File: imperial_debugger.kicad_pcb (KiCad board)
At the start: 4 copper layers, 2 x 7.5 mm, 126 parts, among them J1 USB_B_Micro, J2 Conn_01x04_Male, J3 Conn_01x04_Male, J4 Conn_01x04_Male, J5 Conn_01x06_Male, J6 Conn_01x05_Male, J7 Conn_01x05_Male, J8 Conn_01x05_Male, J9 Conn_01x04_Male, U1 LM2594M-3.3, U10 74LVC1G3157, U11 SP330EEY-L, U12 TXS0104EDR, U13 74LVC1G3157, U14 MAX3222EIPW, U2 93LC54B, U3 FT4232H, U4 74LVC1G3157, U5 SP330EEY-L, U6 74LVC1G3157, U7 TLV75525PDBV, U8 TXS0104EDR, U9 TLV75518PDBV, Y1 12MHz

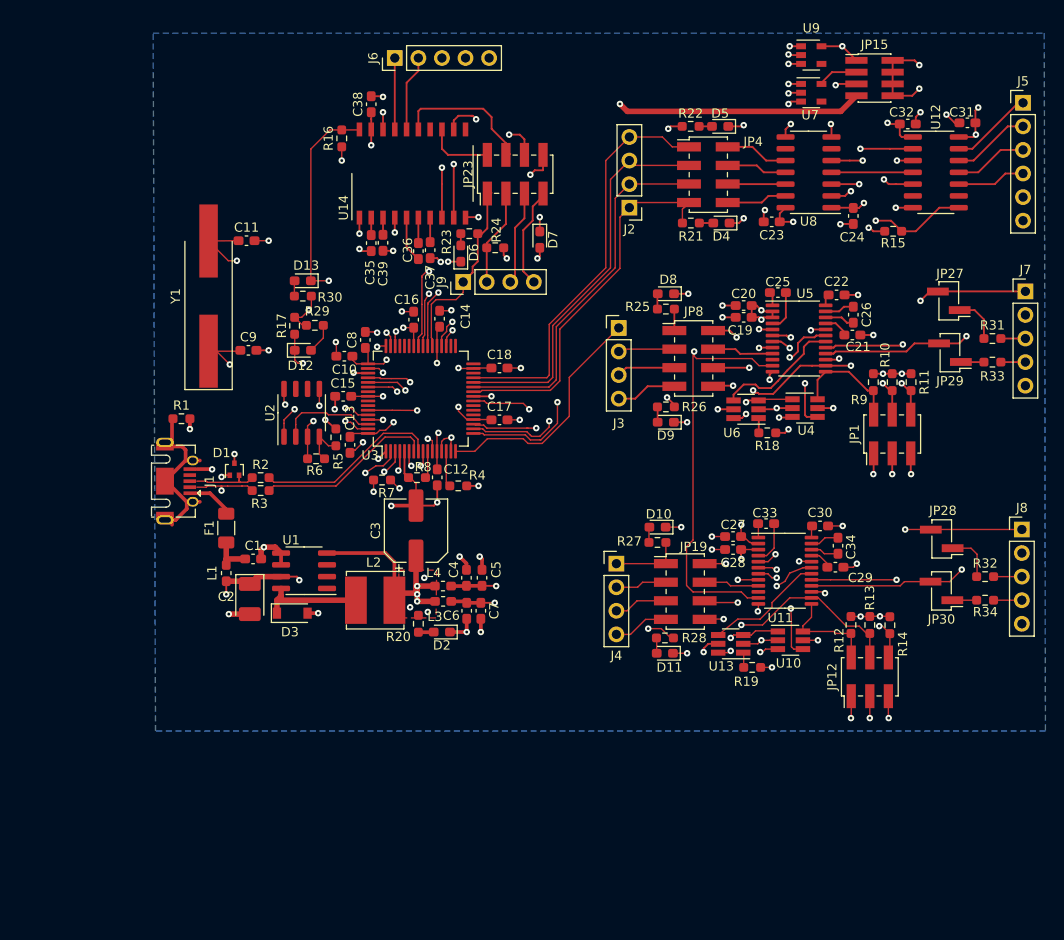
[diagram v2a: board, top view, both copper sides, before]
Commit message: Updates with all the routing and moving to kicad 6.0
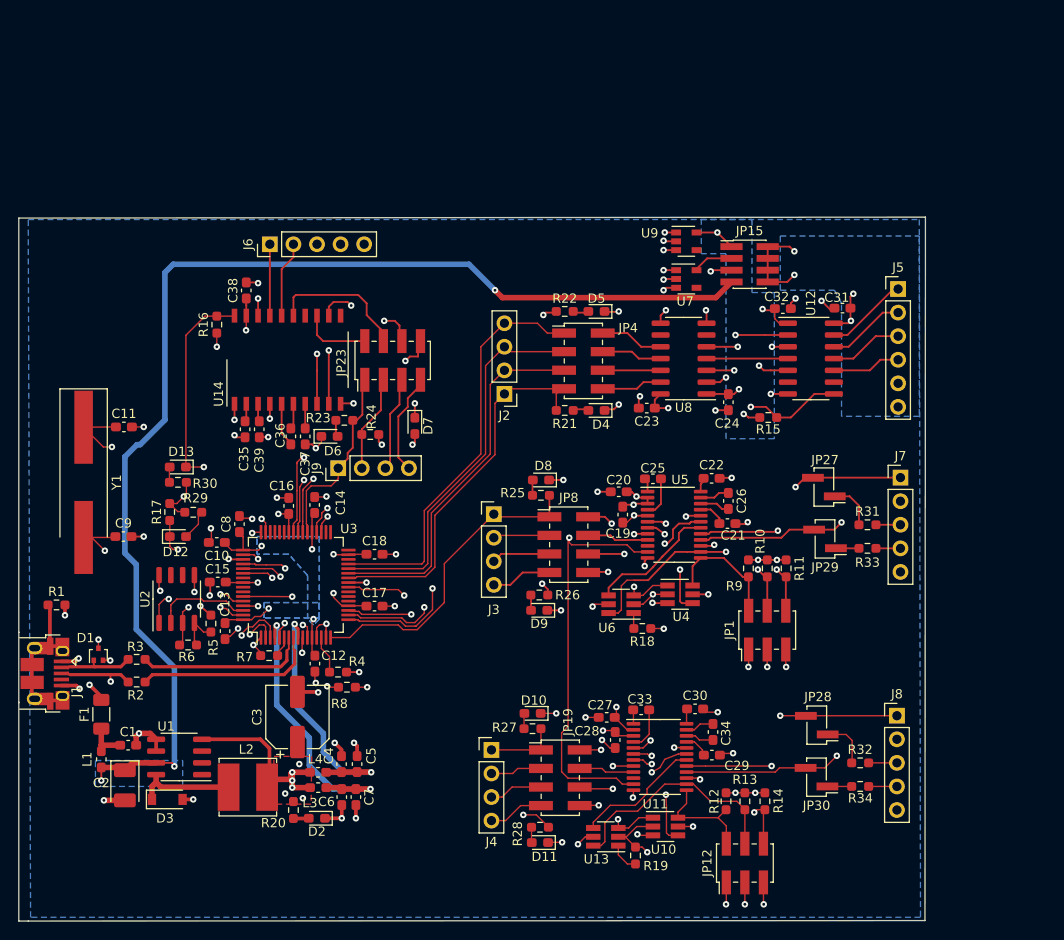
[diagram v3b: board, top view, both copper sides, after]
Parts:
- J1: footprint Connector_USB:USB_Micro-AB_Molex_47590-0001 -> Connector_USB:USB_Micro-B_Amphenol_10103594-0001LF_Horizontal
- moved R2 25.8 mm to (36.8, 127.1)
- moved JP1 25.1 mm to (104.8, 121.5)
- moved R18 25.0 mm to (91.3, 121.3)
- moved U6 24.9 mm to (89.0, 118.7)
- moved C19 24.9 mm to (89.2, 109.0), turned to -90 degrees
- moved U13 24.8 mm to (87.4, 143.7)
- moved D1 24.7 mm to (32.7, 124.1)
- moved J1 24.4 mm to (27.0, 126.2)
- moved R28 24.4 mm to (80.3, 142.7)
- moved D11 24.4 mm to (80.3, 144.3)
- moved D9 24.4 mm to (80.2, 119.3)
- moved R26 24.4 mm to (80.2, 117.7)
- moved C21 24.4 mm to (100.5, 110.0)
- moved L2 24.4 mm to (48.8, 138.4)
- moved R6 24.3 mm to (42.4, 123.1)
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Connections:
- J1 pad 4: Net-(J1-Pad4) -> unconnected-(J1-Pad4)
- U1 pad 1: Net-(U1-Pad1) -> unconnected-(U1-Pad1)
- U1 pad 2: Net-(U1-Pad2) -> unconnected-(U1-Pad2)
- U1 pad 3: Net-(U1-Pad3) -> unconnected-(U1-Pad3)
- U11 pad 10: Net-(U11-Pad10) -> unconnected-(U11-Pad10)
- U2 pad 6: Net-(U2-Pad6) -> unconnected-(U2-Pad6)
- U2 pad 7: Net-(U2-Pad7) -> unconnected-(U2-Pad7)
- U5 pad 10: Net-(U5-Pad10) -> unconnected-(U5-Pad10)
- U7 pad 4: Net-(U7-Pad4) -> unconnected-(U7-Pad4)
- U9 pad 4: Net-(U9-Pad4) -> unconnected-(U9-Pad4)
- Y1 pad 1: Net-(C9-Pad1) -> Net-(C11-Pad1)
- Y1 pad 2: Net-(C11-Pad1) -> Net-(C9-Pad1)
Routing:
- net VPHY: track 7.02 -> 30.7 mm
- net VPLL: track 6.54 -> 27.6 mm
- net Net-(J1-Pad6): track 18.2 -> 12.5 mm
- net ADBUS0: track 28.7 -> 34.4 mm
- net /USB and Power/D+: track 7.02 -> 12.2 mm, vias 0 -> 2
- net Net-(R8-Pad2): track 2.81 -> 7.65 mm, vias 0 -> 2
- net Net-(R7-Pad1): track 6.00 -> 2.24 mm, vias 2 -> 0
- net Net-(F1-Pad2): track 4.35 -> 7.97 mm, vias 0 -> 2
- net GND: track 138.6 -> 141.7 mm, vias 74 -> 72
- net +3V3: track 95.1 -> 92.2 mm
- net Net-(C9-Pad1): track 29.8 -> 31.5 mm
- net Net-(R19-Pad1): track 1.61 -> 3.25 mm
- net CDBUS7: track 1.60 -> 0.00 mm, vias 1 -> 0
- net /USB and Power/D-: track 9.02 -> 10.5 mm, vias 2 -> 0
- net +1V8: track 14.6 -> 13.2 mm
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- added copper zone on B.Cu, net +1V8
- added copper zone on B.Cu, net +3V3
- added copper zone on B.Cu, net /USB and Power/VREGOUT
- added copper zone on In1.Cu, net GND
- added copper zone on B.Cu, net VBUS
- added copper zone on B.Cu, net Vdrive
- removed copper zone on In1.Cu, net +1V8
- removed copper zone on In1.Cu, net +3V3
- removed copper zone on In1.Cu, net /USB and Power/VREGOUT
- removed copper zone on B.Cu, net GND
- removed copper zone on In1.Cu, net VBUS
- removed copper zone on In1.Cu, net VPHY
- removed copper zone on In1.Cu, net VPLL
- removed copper zone on In1.Cu, net Vdrive
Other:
- board size 2 x 7.5 mm -> 97.7 x 75.8 mm
- net class Default removed
- net class Power removed
- net class USB removed

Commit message: After update to kicak 9.0
Signed-off-by: Marc Kelly <mpkelly@achenar.co.uk>
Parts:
- added FID1: Fiducial, Fiducial:Fiducial_1.5mm_Mask3mm, F.Cu at (35.6, 90.3)
- added FID2: Fiducial, Fiducial:Fiducial_1.5mm_Mask3mm, F.Cu at (88.3, 81.9)
- added FID3: Fiducial, Fiducial:Fiducial_1.5mm_Mask3mm, F.Cu at (109.8, 145.7)
- added H1: MountingHole, MountingHole:MountingHole_3.2mm_M3, F.Cu at (32.4, 183.4)
- added H2: MountingHole, MountingHole:MountingHole_3.2mm_M3, F.Cu at (40.4, 183.4)
- added H3: MountingHole, MountingHole:MountingHole_3.2mm_M3, F.Cu at (40.4, 175.5)
- added H4: MountingHole, MountingHole:MountingHole_3.2mm_M3, F.Cu at (32.4, 175.5)
- R10, R11, R12, R13, R14, R9: value 4.7k -> 4k7
- R3: value R10 -> 10R

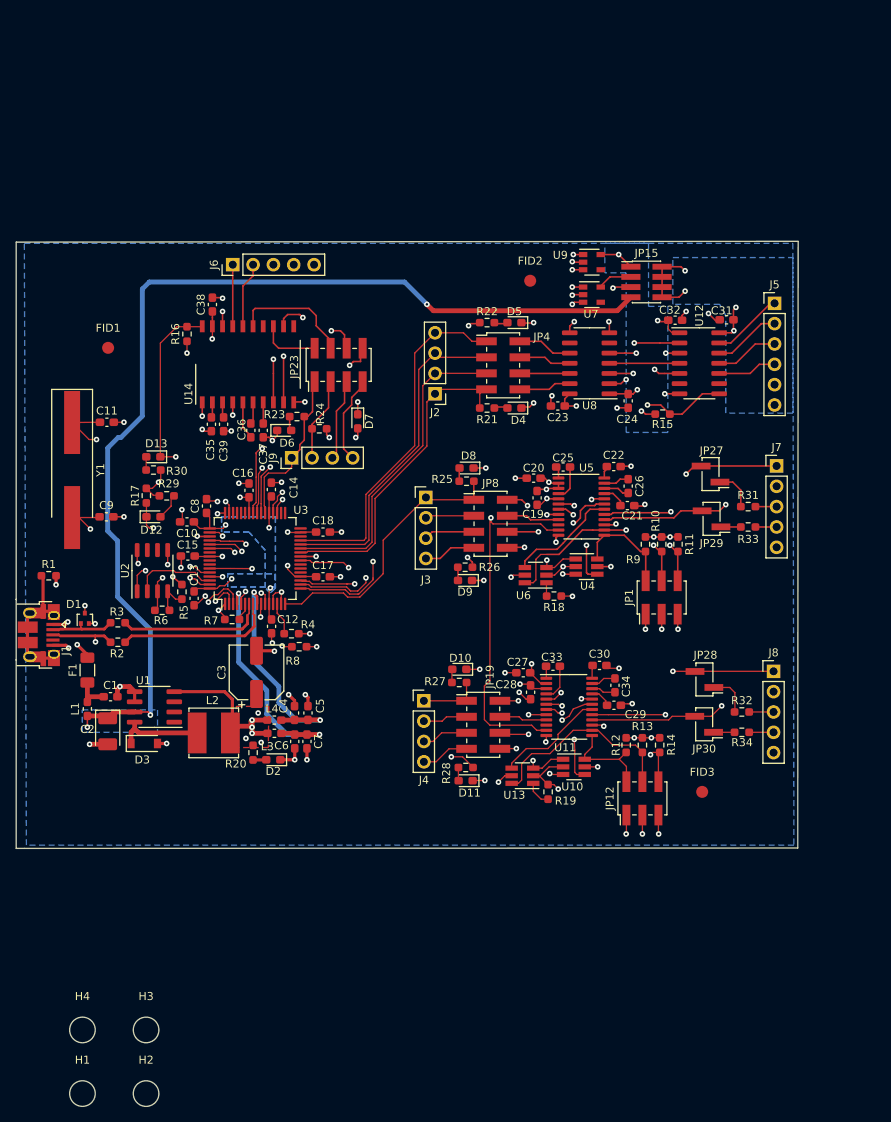
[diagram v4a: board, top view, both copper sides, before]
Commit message: Updated with the new design.
Removed all level translators.
4 sockets, 2x6 pin outputs
New PCB shape and routing
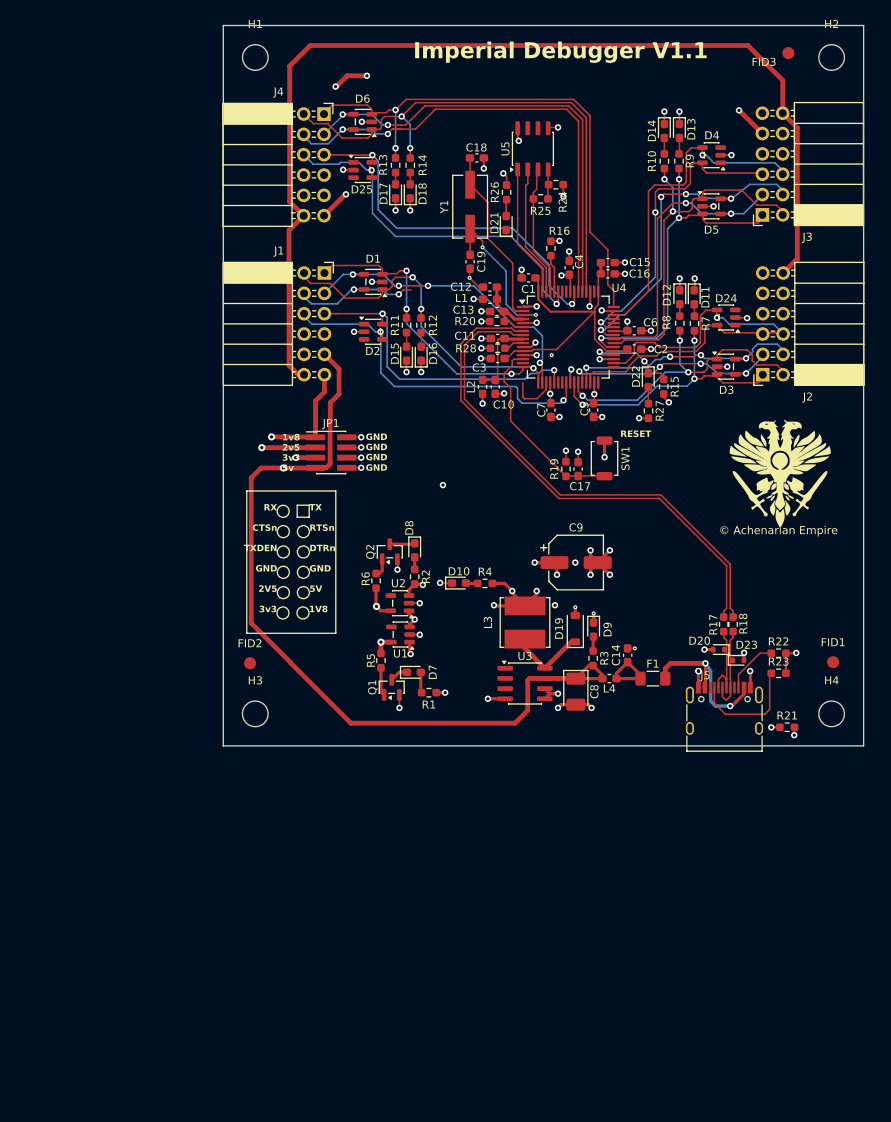
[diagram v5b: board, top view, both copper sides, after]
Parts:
- removed C20, C21, C22, C23, C24, C25, C26, C27, C28, C29, C30, C31, C32, C33, C34, C35, C36, C37, C38, C39: 100nF, Capacitor_SMD:C_0603_1608Metric_Pad1.08x0.95mm_HandSolder
- removed J6, J7, J8: Conn_01x05_Male, Connector_PinHeader_2.54mm:PinHeader_1x05_P2.54mm_Vertical
- removed J9: Conn_01x04_Male, Connector_PinHeader_2.54mm:PinHeader_1x04_P2.54mm_Vertical
- removed JP12: Jumper, Connector_PinHeader_2.00mm:PinHeader_2x03_P2.00mm_Vertical_SMD
- removed JP15: Jumper, Connector_PinHeader_1.27mm:PinHeader_2x04_P1.27mm_Vertical_SMD
- removed JP19, JP23, JP4, JP8: Jumper, Connector_PinHeader_2.00mm:PinHeader_2x04_P2.00mm_Vertical_SMD
- removed JP27, JP28, JP29, JP30: Jumper, Connector_PinHeader_2.00mm:PinHeader_1x02_P2.00mm_Vertical_SMD_Pin1Left
- removed R29, R30: 330R, Resistor_SMD:R_0603_1608Metric_Pad0.98x0.95mm_HandSolder
- removed R31, R32, R33, R34: 120R, Resistor_SMD:R_0603_1608Metric_Pad0.98x0.95mm_HandSolder
- removed U10, U13, U6: 74LVC1G3157, Package_TO_SOT_SMD:SOT-23-6_Handsoldering
- removed U11: SP330EEY-L, Package_SO:TSSOP-24_4.4x7.8mm_P0.65mm
- removed U12, U8: TXS0104EDR, Package_SO:SOIC-14_3.9x8.7mm_P1.27mm
- removed U14: MAX3222EIPW, Package_SO:SO-20_12.8x7.5mm_P1.27mm
- removed U7: TLV75525PDBV, Package_TO_SOT_SMD:SOT-23-5
- removed U9: TLV75518PDBV, Package_TO_SOT_SMD:SOT-23-5
- added D14: G_LED, LED_SMD:LED_0603_1608Metric_Pad1.05x0.95mm_HandSolder, F.Cu at (105.1, 63.2)
- added D15: G_LED, LED_SMD:LED_0603_1608Metric_Pad1.05x0.95mm_HandSolder, F.Cu at (72.9, 91.0)
- added D16: G_LED, LED_SMD:LED_0603_1608Metric_Pad1.05x0.95mm_HandSolder, F.Cu at (74.7, 91.0)
- added D17: G_LED, LED_SMD:LED_0603_1608Metric_Pad1.05x0.95mm_HandSolder, F.Cu at (71.5, 70.7)
- added D18: G_LED, LED_SMD:LED_0603_1608Metric_Pad1.05x0.95mm_HandSolder, F.Cu at (73.4, 70.7)
- added D19: 1A 20V, Diode_SMD:D_SOD-123, F.Cu at (94.0, 125.3)
- added D20: ESD5Zxx, Diode_SMD:D_SOD-523, F.Cu at (111.9, 128.0)
- added D21: G_LED, LED_SMD:LED_0603_1608Metric_Pad1.05x0.95mm_HandSolder, F.Cu at (85.3, 74.7)
- added D22: Or_LED, LED_SMD:LED_0603_1608Metric_Pad1.05x0.95mm_HandSolder, F.Cu at (103.1, 94.3)
- added D23: ESD5Zxx, Diode_SMD:D_SOD-523, F.Cu at (114.4, 129.3)
- added D24: ESDS304, Package_TO_SOT_SMD:SOT-23-5, F.Cu at (112.8, 86.5)
- added D25: ESDS304, Package_TO_SOT_SMD:SOT-23-5, F.Cu at (67.4, 68.1)
- added LOGO1: ~, Achenar_Logos:achenar_logo, F.Cu at (119.5, 106.0)
- added Q1: SI500N025UK-TP, Package_TO_SOT_SMD:SOT-23, F.Cu at (71.0, 132.7)
- added Q2: SI500N025UK-TP, Package_TO_SOT_SMD:SOT-23, F.Cu at (70.8, 115.7)
- added SW1: ResetButton, Button_Switch_SMD:SW_SPST_TS-1088-xR020, F.Cu at (97.6, 104.1)
- C1: value 10nf -> 100nF
- C10, C12: value 100nF -> 4.7uF
- C14: value 100nF -> 10nf
- C16: value 100nF -> 3.3uF
- C2: value 68uF -> 100nF; footprint Capacitor_Tantalum_SMD:CP_EIA-3528-21_Kemet-B_Pad1.50x2.35mm_HandSolder -> Capacitor_SMD:C_0603_1608Metric_Pad1.08x0.95mm_HandSolder
- C3: value 120uF -> 100nF; footprint Capacitor_SMD:CP_Elec_6.3x5.7 -> Capacitor_SMD:C_0603_1608Metric_Pad1.08x0.95mm_HandSolder
- C4, C6: value 4.7uF -> 100nF
- C8: value 3.3uF -> 68uF; footprint Capacitor_SMD:C_0603_1608Metric_Pad1.08x0.95mm_HandSolder -> Capacitor_Tantalum_SMD:CP_EIA-3528-21_Kemet-B_HandSolder
- C9: value 100nF -> 120uF; footprint Capacitor_SMD:C_0603_1608Metric_Pad1.08x0.95mm_HandSolder -> Capacitor_SMD:CP_Elec_6.3x5.7
- D1: value RClamp0582BQ -> ESDS304; footprint Package_TO_SOT_SMD:SOT-416 -> Package_TO_SOT_SMD:SOT-23-5
- D10, D7, D8, D9: value G_LED -> Y_LED
- D13: value Or_LED -> G_LED
- D2, D4, D5, D6: value G_LED -> ESDS304; footprint LED_SMD:LED_0603_1608Metric_Pad1.05x0.95mm_HandSolder -> Package_TO_SOT_SMD:SOT-23-5
- D3: value 1A 20V -> ESDS304; footprint Diode_SMD:D_SOD-123 -> Package_TO_SOT_SMD:SOT-23-5
- J1: value USB_B_Micro -> Conn_02x06_Odd_Even; footprint Connector_USB:USB_Micro-B_Amphenol_10103594-0001LF_Horizontal -> Connector_PinSocket_2.54mm:PinSocket_2x06_P2.54mm_Horizontal
- J2, J3, J4: value Conn_01x04_Male -> Conn_02x06_Odd_Even; footprint Connector_PinHeader_2.54mm:PinHeader_1x04_P2.54mm_Vertical -> Connector_PinSocket_2.54mm:PinSocket_2x06_P2.54mm_Horizontal
- J5: value Conn_01x06_Male -> USB_C_Receptacle_USB2.0_14P; footprint Connector_PinHeader_2.54mm:PinHeader_1x06_P2.54mm_Vertical -> Connector_USB:USB_C_Receptacle_HRO_TYPE-C-31-M-12
- JP1: footprint Connector_PinHeader_2.00mm:PinHeader_2x03_P2.00mm_Vertical_SMD -> Connector_PinHeader_1.27mm:PinHeader_2x04_P1.27mm_Vertical_SMD
- L2: value SRN6045-101M -> 330R/0.5A; footprint Inductor_SMD:L_Bourns_SRN6045TA -> Inductor_SMD:L_0603_1608Metric_Pad1.05x0.95mm_HandSolder
- L3: value 330R/0.5A -> SRN6045-101M; footprint Inductor_SMD:L_0603_1608Metric_Pad1.05x0.95mm_HandSolder -> Inductor_SMD:L_Bourns_SRN6045TA
- R1, R8: value 0R -> 330R
- R10, R11, R12, R13, R14, R9: value 4k7 -> 330R
- R17, R18: value 4k7 -> 10R
- R19: value 4k7 -> 10k
- R2, R3: value 10R -> 330R
- R20: value 330R -> 12k/1%
- R21, R28: value 330R -> 0R
- R22, R23: value 330R -> 5k1
- R24: value 330R -> 10k
- R25: value 330R -> 2K
- R4, R5: value 10k -> 330R
- R6: value 2K -> 330R
- R7: value 12k/1% -> 330R
- U1: value LM2594M-3.3 -> TLV75525PDBV; footprint Package_SO:SOIC-8_3.9x4.9mm_P1.27mm -> Package_TO_SOT_SMD:SOT-23-5
- U2: value 93LC54B -> TLV75518PDBV; footprint Package_SO:SO-8_3.9x4.9mm_P1.27mm -> Package_TO_SOT_SMD:SOT-23-5
- U3: value FT4232H -> LM2594M-3.3; footprint Package_QFP:LQFP-64_10x10mm_P0.5mm -> Package_SO:SOIC-8_3.9x4.9mm_P1.27mm
- U4: value 74LVC1G3157 -> FT4232H; footprint Package_TO_SOT_SMD:SOT-23-6_Handsoldering -> Package_QFP:LQFP-64_10x10mm_P0.5mm
- U5: value SP330EEY-L -> 93LC54B; footprint Package_SO:TSSOP-24_4.4x7.8mm_P0.65mm -> Package_SO:SO-8_3.9x4.9mm_P1.27mm
- Y1: value 12MHz -> ABLS7M2-12.000MHZ-D2Y-T; footprint Crystal:Crystal_SMD_HC49-SD_HandSoldering -> Crystal:Crystal_SMD_ECS_CSM3X-2Pin_7.6x4.1mm
- moved H2 155.2 mm to (126.0, 54.0)
- moved H1 131.2 mm to (54.0, 54.0)
- moved H4 101.6 mm to (126.0, 136.0)
- moved FID1 98.7 mm to (126.2, 129.5)
- moved FID3 92.9 mm to (120.6, 53.4), turned to -90 degrees
- moved D3 86.6 mm to (112.8, 92.6)
- moved C2 81.3 mm to (101.3, 90.4), turned to 0 degrees
- moved R14 78.9 mm to (73.4, 67.5), turned to 90 degrees
- moved R13 78.7 mm to (71.5, 67.5), turned to 90 degrees
- moved D13 77.3 mm to (107.0, 63.2), turned to -90 degrees
- moved J4 74.4 mm to (62.6, 61.1)
- moved C1 73.9 mm to (88.1, 81.5), turned to 180 degrees
- moved R17 73.9 mm to (112.5, 124.8)
- moved L1 71.8 mm to (83.3, 84.2), turned to 0 degrees
- moved D12 71.3 mm to (107.0, 83.9), turned to -90 degrees
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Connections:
- C1 pad 1: Net-(C1-Pad1) -> /USB and Power/VREGOUT
- C10 pad 1: /USB and Power/VREGOUT -> VPLL
- C11 pad 1: Net-(C11-Pad1) -> VPLL
- C12 pad 1: /USB and Power/VREGOUT -> VPHY
- C13 pad 1: /USB and Power/VREGOUT -> VPHY
- C14 pad 1: /USB and Power/VREGOUT -> Net-(C14-Pad1)
- C15 pad 1: +3V3 -> /USB and Power/VREGOUT
- C16 pad 1: +3V3 -> /USB and Power/VREGOUT
- C17 pad 1: +3V3 -> /USB and Power/RESET#
- C18 pad 1: +3V3 -> Net-(U4-OSCI)
- C19 pad 1: +3V3 -> Net-(U4-OSCO)
- C2 pad 1: VBUS -> /USB and Power/VREGOUT
- C3 pad 1: +3V3 -> /USB and Power/VREGOUT
- C4 pad 1: VPLL -> +3V3
- C5 pad 1: VPLL -> +3V3
- C6 pad 1: VPHY -> +3V3
- C7 pad 1: VPHY -> +3V3
- C8 pad 1: /USB and Power/VREGOUT -> VBUS
- C9 pad 1: Net-(C9-Pad1) -> +3V3
- D1 pad 1: /USB and Power/D- -> ADBUS1
- D1 pad 2: /USB and Power/D+ -> GND
- D1 pad 3: GND -> ADBUS0
- D10 pad 2: Net-(D10-Pad2) -> Net-(D10-A)
- D11 pad 2: Net-(D11-Pad2) -> Net-(D11-A)
- D12 pad 1: PWREN# -> GND
- D12 pad 2: Net-(D12-Pad2) -> Net-(D12-A)
- D13 pad 1: SUSPEND# -> GND
- D13 pad 2: Net-(D13-Pad2) -> Net-(D13-A)
- D2 pad 1: GND -> unconnected-(D2-K-Pad1)
- D2 pad 2: Net-(D2-Pad2) -> GND
- D3 pad 1: Net-(D3-Pad1) -> BDBUS1
- D4 pad 1: GND -> unconnected-(D4-K-Pad1)
- D4 pad 2: Net-(D4-Pad2) -> GND
- D5 pad 1: GND -> CDBUS1
- D5 pad 2: Net-(D5-Pad2) -> GND
- D6 pad 1: GND -> DDBUS1
- D6 pad 2: Net-(D6-Pad2) -> GND
- D7 pad 1: GND -> Net-(D7-K)
- D7 pad 2: Net-(D7-Pad2) -> Net-(D7-A)
- D8 pad 1: GND -> Net-(D8-K)
- D8 pad 2: Net-(D8-Pad2) -> Net-(D8-A)
- D9 pad 2: Net-(D9-Pad2) -> Net-(D9-A)
- F1 pad 1: Net-(C1-Pad1) -> Net-(C14-Pad1)
- J1 pad 1: Net-(F1-Pad2) -> ADBUS0
- J1 pad 2: /USB and Power/D- -> ADBUS1
- J1 pad 3: /USB and Power/D+ -> ADBUS2
- J1 pad 4: unconnected-(J1-Pad4) -> ADBUS3
- J1 pad 5: GND -> ADBUS4
- J1 pad 6: Net-(J1-Pad6) -> ADBUS7
- J3 pad 1: ADBUS0 -> CDBUS0
- J3 pad 2: ADBUS1 -> CDBUS1
- J3 pad 3: ADBUS2 -> CDBUS2
- J3 pad 4: ADBUS3 -> CDBUS3
- JP1 pad 1: GND -> +1V8
- JP1 pad 2: /Transceivers/RS323n_3 -> GND
- JP1 pad 3: GND -> +2V5
- JP1 pad 4: /Transceivers/FULLn_3 -> GND
- JP1 pad 5: GND -> +3V3
- JP1 pad 6: Net-(JP1-Pad6) -> GND
- L1 pad 1: VBUS -> +3V3
- L1 pad 2: Net-(C1-Pad1) -> VPHY
- L2 pad 1: Net-(D3-Pad1) -> +3V3
- L2 pad 2: +3V3 -> VPLL
- L3 pad 1: +3V3 -> Net-(D19-K)
- L3 pad 2: VPHY -> +3V3
- L4 pad 1: +3V3 -> VBUS
- L4 pad 2: VPLL -> Net-(C14-Pad1)
- R1 pad 1: Net-(J1-Pad6) -> Net-(D7-A)
- R1 pad 2: GND -> +3V3
- R10 pad 1: +3V3 -> Net-(D14-A)
- R10 pad 2: /Transceivers/FULLn_3 -> CDBUS1
- R11 pad 1: +3V3 -> Net-(D15-A)
- R11 pad 2: Net-(JP1-Pad6) -> ADBUS0
- R12 pad 1: +3V3 -> Net-(D16-A)
- R12 pad 2: /Transceivers/RS323n_4 -> ADBUS1
- R13 pad 1: +3V3 -> Net-(D17-A)
- R13 pad 2: /Transceivers/FULLn_4 -> DDBUS0
- R14 pad 1: +3V3 -> Net-(D18-A)
- R14 pad 2: Net-(JP12-Pad6) -> DDBUS1
- R15 pad 1: +1V8 -> +3V3
- R15 pad 2: Net-(R15-Pad2) -> SUSPEND#
- R16 pad 2: SUSPEND# -> PWREN#
- R17 pad 1: +3V3 -> /USB and Power/D_N
- R17 pad 2: PWREN# -> /USB and Power/D-
- R18 pad 1: Net-(R18-Pad1) -> /USB and Power/D_P
- R18 pad 2: GND -> /USB and Power/D+
- R19 pad 1: Net-(R19-Pad1) -> /USB and Power/RESET#
- R19 pad 2: GND -> +3V3
- R2 pad 1: /USB and Power/D_P -> Net-(D8-A)
- R2 pad 2: /USB and Power/D+ -> +3V3
- R20 pad 1: Net-(D2-Pad2) -> Net-(U4-REF)
- R20 pad 2: +3V3 -> GND
- R21 pad 1: Net-(D4-Pad2) -> Net-(J5-SHIELD)
- R21 pad 2: BDBUS0 -> GND
- R22 pad 1: Net-(D5-Pad2) -> Net-(J5-CC2)
- R22 pad 2: BDBUS1 -> GND
- R23 pad 1: Net-(D6-Pad2) -> Net-(J5-CC1)
- R23 pad 2: CDBUS0 -> GND
- R24 pad 1: Net-(D7-Pad2) -> Net-(U5-DO)
- R24 pad 2: CDBUS1 -> +3V3
- R25 pad 1: Net-(D8-Pad2) -> Net-(U4-EEDATA)
- R25 pad 2: ADBUS0 -> Net-(U5-DO)
- R26 pad 1: Net-(D9-Pad2) -> Net-(D21-A)
- R26 pad 2: ADBUS1 -> +3V3
- R27 pad 1: Net-(D10-Pad2) -> Net-(D22-A)
- R27 pad 2: DDBUS0 -> +3V3
- R28 pad 1: Net-(D11-Pad2) -> GND
- R28 pad 2: DDBUS1 -> Net-(U4-AGND)
- R3 pad 1: /USB and Power/D_N -> Net-(D9-A)
- R3 pad 2: /USB and Power/D- -> VBUS
- R4 pad 1: /USB and Power/RESET# -> Net-(D10-A)
- R5 pad 1: Net-(R5-Pad1) -> +2V5
- R5 pad 2: +3V3 -> Net-(Q1-G)
- R6 pad 1: Net-(R6-Pad1) -> +1V8
- R6 pad 2: Net-(R5-Pad1) -> Net-(Q2-G)
- R7 pad 1: Net-(R7-Pad1) -> Net-(D11-A)
- R7 pad 2: GND -> BDBUS0
- R8 pad 1: GND -> Net-(D12-A)
- R8 pad 2: Net-(R8-Pad2) -> BDBUS1
- R9 pad 1: +3V3 -> Net-(D13-A)
- R9 pad 2: /Transceivers/RS323n_3 -> CDBUS0
- U1 pad 1: unconnected-(U1-Pad1) -> +3V3
- U1 pad 2: unconnected-(U1-Pad2) -> GND
- U1 pad 3: unconnected-(U1-Pad3) -> +3V3
- U1 pad 4: +3V3 -> unconnected-(U1-NC-Pad4)
- U1 pad 5: GND -> +2V5
- U2 pad 1: Net-(U2-Pad1) -> +3V3
- U2 pad 2: Net-(U2-Pad2) -> GND
- U2 pad 3: Net-(R6-Pad1) -> +3V3
- U2 pad 4: Net-(R5-Pad1) -> unconnected-(U2-NC-Pad4)
- U2 pad 5: GND -> +1V8
- U3 pad 1: GND -> unconnected-(U3-NC-Pad1)
- U3 pad 2: Net-(C9-Pad1) -> unconnected-(U3-NC-Pad2)
- U3 pad 3: Net-(C11-Pad1) -> unconnected-(U3-NC-Pad3)
- U3 pad 4: VPHY -> +3V3
- U3 pad 6: Net-(R7-Pad1) -> GND
- U3 pad 7: /USB and Power/D_N -> VBUS
- U3 pad 8: /USB and Power/D_P -> Net-(D19-K)
- U4 pad 1: ADBUS7 -> GND
- U4 pad 2: GND -> Net-(U4-OSCI)
- U4 pad 3: /Transceivers/RTSn_3 -> Net-(U4-OSCO)
- U4 pad 4: /Transceivers/T2IN_3 -> VPHY
- U4 pad 5: +3V3 -> GND
- U4 pad 6: /Transceivers/RS323n_3 -> Net-(U4-REF)
- U5 pad 1: Net-(C25-Pad2) -> Net-(U4-EECS)
- U5 pad 2: +3V3 -> Net-(U4-EECLK)
- U5 pad 3: +3V3 -> Net-(U4-EEDATA)
- U5 pad 4: Net-(C25-Pad1) -> Net-(U5-DO)
- U5 pad 6: /Transceivers/PORT_3_TXD -> unconnected-(U5-NC-Pad6)
- U5 pad 7: /Transceivers/PORT_3_RTS -> unconnected-(U5-NC-Pad7)
- U5 pad 8: /Transceivers/CTSn_3 -> +3V3
- Y1 pad 1: Net-(C11-Pad1) -> Net-(U4-OSCO)
- Y1 pad 2: Net-(C9-Pad1) -> Net-(U4-OSCI)
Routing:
- net +2V5: track 4.37 -> 193.8 mm, vias 0 -> 2
- net +1V8: track 13.2 -> 173.0 mm, vias 4 -> 3
- net +3V3: track 92.2 -> 215.9 mm, vias 35 -> 27
- net SUSPEND#: track 112.2 -> 12.3 mm, vias 3 -> 2
- net VBUS: track 131.0 -> 221.5 mm, vias 3 -> 4
- net DDBUS4: track 0.00 -> 46.5 mm, vias 0 -> 2
- net /USB and Power/D_N: track 18.4 -> 64.1 mm
- net /USB and Power/D_P: track 19.8 -> 63.4 mm
- net Net-(C11-Pad1): track 42.8 -> 0.00 mm, vias 2 -> 0
- net CDBUS7: track 0.00 -> 40.9 mm, vias 0 -> 1
- net ADBUS4: track 0.00 -> 39.0 mm, vias 0 -> 2
- net CDBUS4: track 0.00 -> 38.8 mm, vias 0 -> 2
- net GND: track 141.7 -> 106.9 mm, vias 72 -> 69
- net /Transceivers/PORT_4_RTS: track 32.5 -> 0.00 mm, vias 1 -> 0
- net /Transceivers/PORT_3_RTS: track 31.8 -> 0.00 mm, vias 1 -> 0
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- added copper zone on In2.Cu, net +3V3
- added copper zone on In1.Cu, net Net-(J5-SHIELD)
- removed copper zone on B.Cu, net +1V8
- removed copper zone on B.Cu, net +3V3
- removed copper zone on F.Cu, net +3V3
- removed copper zone on B.Cu, net /USB and Power/VREGOUT
- removed copper zone on B.Cu, net VBUS
- removed copper zone on B.Cu, net Vdrive
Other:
- board size 97.7 x 75.8 mm -> 80 x 90 mm
- board text added: "1V8"
- board text added: "1v8"
- board text added: "2V5"
- board text added: "2v5"
- board text added: "3v3"
- board text added: "5V"
- board text added: "5v"
- board text added: "CTSn"
- board text added: "DTRn"
- board text added: "GND"
- board text added: "Imperial Debugger V${REVISION}"
- board text added: "RESET"
- board text added: "RTSn"
- board text added: "RX"
- board text added: "TX"
- board text added: "TXDEN"

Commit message: Add some info to the master document
Signed-off-by: Marc Kelly <mpkelly@achenar.co.uk>
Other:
- board text added: "Sub Module need to be 15.3+4.6 = 19.9 mm So will go for 19.4 mm wide for the sub modules."
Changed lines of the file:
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@@
+	)
+	(gr_rect
+		(start 145.4404 77.5994)
+		(end 195.4404 96.9994)
+		(stroke
+			(width 0.1)
+			(type solid)
+		)
+		(fill no)
+		(layer "Dwgs.User")
+	)
+	(gr_rect
+		(start 145.434 57.635)
+		(end 195.434 77.035)
+		(stroke
+			(width 0.1)
+			(type solid)
+		)
+		(fill no)
+		(layer "Dwgs.User")
 	)
 	(gr_rect
@@
 		)
 	)
+	(gr_text "Sub Module need to be 15.3+4.6 = 19.9 mm\n So will go for 19.4 mm wide for the sub modules."
+		(at 136.2964 56.769 0)
+		(layer "Dwgs.User")
+		(effects
+			(font
+				(size 1 1)
+				(thickness 0.15)
+			)
+			(justify left bottom)
+		)
+	)
+	(dimension
+		(type orthogonal)
+		(layer "Dwgs.User")
+		(pts
+			(xy 135.7376 74.99) (xy 136.61004 59.610569)
+		)
+		(height 0)
+		(orientation 1)
+		(format
+			(prefix "")
+			(suffix "")
+			(units 3)
+			(units_format 1)
+			(precision 4)
+		)
+		(style
+			(thickness 0.1)
+			(arrow_length 1.27)
+			(text_position_mode 0)
+			(arrow_direction outward)
+			(extension_height 0.58642)
+			(extension_offset 0.5)
+			(keep_text_aligned yes)
+		)
+		(gr_text "15.3794 mm"
+			(at 134.5876 67.300284 90)
+			(layer "Dwgs.User")
+			(effects
+				(font
+					(size 1 1)
+					(thickness 0.15)
+				)
+			)
+		)
+	)
+	(dimension
+		(type orthogonal)
+		(layer "Dwgs.User")
+		(pts
+			(xy 133.479591 79.5944) (xy 133.618874 74.99)
+		)
+		(height 0)
+		(orientation 1)
+		(format
+			(prefix "")
+			(suffix "")
+			(units 3)
+			(units_format 1)
+			(precision 4)
+		)
+		(style
+			(thickness 0.1)
+			(arrow_length 1.27)
+			(text_position_mode 0)
+			(arrow_direction outward)
+			(extension_height 0.58642)
+			(extension_offset 0.5)
+			(keep_text_aligned yes)
+		)
+		(gr_text "4.6044 mm"
+			(at 132.329591 77.2922 90)
+			(layer "Dwgs.User")
+			(effects
+				(font
+					(size 1 1)
+					(thickness 0.15)
+				)
+			)
+		)
+	)
+	(dimension
+		(type orthogonal)
+		(layer "Dwgs.User")
+		(pts
+			(xy 195.4404 77.5994) (xy 195.434 77.035)
+		)
+		(height 2.1462)
+		(orientation 1)
+		(format
+			(prefix "")
+			(suffix "")
+			(units 3)
+			(units_format 1)
+			(precision 4)
+		)
+		(style
+			(thickness 0.1)
+			(arrow_length 1.27)
+			(text_position_mode 0)
+			(arrow_direction outward)
+			(extension_height 0.58642)
+			(extension_offset 0.5)
+			(keep_text_aligned yes)
+		)
+		(gr_text "0.5644 mm"
+			(at 196.4366 77.3172 90)
+			(layer "Dwgs.User")
+			(effects
+				(font
+					(size 1 1)
+					(thickness 0.15)
+				)
+			)
+		)
+	)
